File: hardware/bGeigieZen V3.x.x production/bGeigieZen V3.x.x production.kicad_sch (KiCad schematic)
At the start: 14 parts, among them J1 M5 2x15 pin, J10 QI GND, J11 QI charger Plus, J2 Geiger IRover, J3 GPS, J4 Geiger Safepulse, J5 Extra support header, J6 Grove, J8 QI charger ground, J9 QI Plus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

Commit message: Changed the 18650 battery holder to a 1043 Keystone and modified the layout.
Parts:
- BT1: footprint Library:BATTERY_18650-HOLDER -> bGeigieZen:1043
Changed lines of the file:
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@@
 			)
 		)
-		(property "Footprint" "Library:BATTERY_18650-HOLDER"
+		(property "Footprint" "bGeigieZen:1043"
 			(at 83.185 102.108 0)
 			(effects

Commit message: Updated SCL and SDA  and fixed labels  RXs and TX2
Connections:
- net RX2: now also J1.16 (Pin_16), J3.3 (Pin_3); no longer J1.15 (Pin_15), J3.4 (Pin_4)
- net SCL: now also J1.17 (Pin_17), J3.1 (Pin_1); no longer J1.18 (Pin_18), J3.6 (Pin_6)
- net SDA: now also J1.18 (Pin_18), J3.6 (Pin_6); no longer J1.17 (Pin_17), J3.1 (Pin_1)
- net TX2: now also J1.15 (Pin_15), J3.4 (Pin_4); no longer J1.16 (Pin_16), J3.3 (Pin_3)
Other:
- title: bGeigieZen V3.0.3 -> bGeigieZen V3.0.5
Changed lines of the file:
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@@
 	(paper "A4")
 	(title_block
-		(title "bGeigieZen V3.0.3")
-		(date "2024-02-06")
-		(rev "V3.0.3")
+		(title "bGeigieZen V3.0.5")
+		(date "2024-04-07")
+		(rev "V3.0.5")
 		(company "GitHub link at https://github.com/Safecast/bGeigieZen")
 	)
@@
 		(at 125.73 125.73)
 		(diameter 0.3048)
+		(color 0 0 0 0)
+	)
+	(junction
+		(at 173.99 92.71)
+		(diameter 0)
 		(color 0 0 0 0)
 	)
@@
 	)
 	(junction
+		(at 171.45 95.25)
+		(diameter 0)
+		(color 0 0 0 0)
+	)
+	(junction
 		(at 135.89 125.73)
 		(diameter 0.3048)
@@
 	)
 	(junction
-		(at 173.99 95.25)
-		(diameter 0)
-		(color 0 0 0 0)
-	)
-	(junction
-		(at 171.45 92.71)
-		(diameter 0)
-		(color 0 0 0 0)
-	)
-	(junction
 		(at 130.81 78.74)
 		(diameter 0.3048)
@@
 	(wire
 		(pts
-			(xy 173.99 85.09) (xy 173.99 95.25)
+			(xy 173.99 85.09) (xy 173.99 92.71)
 		)
 		(stroke
@@
 	(wire
 		(pts
+			(xy 173.99 92.71) (xy 173.99 96.52)
+		)
+		(stroke
+			(width 0)
+			(type default)
+		)
+	)
+	(wire
+		(pts
 			(xy 74.295 85.09) (xy 83.185 85.09)
 		)
@@
 	(wire
 		(pts
+			(xy 171.45 95.25) (xy 184.15 95.25)
+		)
+		(stroke
+			(width 0)
+			(type default)
+		)
+	)
+	(wire
+		(pts
 			(xy 130.81 78.74) (xy 133.35 78.74)
 		)
@@
 	(wire
 		(pts
+			(xy 171.45 95.25) (xy 171.45 120.65)
+		)
+		(stroke
+			(width 0)
+			(type default)
+		)
+	)
+	(wire
+		(pts
 			(xy 133.35 104.14) (xy 131.445 104.14)
 		)
@@
 	(wire
 		(pts
-			(xy 173.99 95.25) (xy 184.15 95.25)
-		)
-		(stroke
-			(width 0)
-			(type default)
-		)
-	)
-	(wire
-		(pts
 			(xy 113.03 78.74) (xy 116.84 78.74)
 		)
@@
 	(wire
 		(pts
-			(xy 173.99 95.25) (xy 173.99 96.52)
-		)
-		(stroke
-			(width 0)
-			(type default)
-		)
-	)
-	(wire
-		(pts
 			(xy 185.42 56.515) (xy 185.42 66.04)
 		)
@@
 	(wire
 		(pts
-			(xy 171.45 92.71) (xy 171.45 72.39)
-		)
-		(stroke
-			(width 0)
-			(type default)
-		)
-	)
-	(wire
-		(pts
 			(xy 74.295 80.01) (xy 74.295 85.09)
 		)
@@
 	(wire
 		(pts
-			(xy 171.45 92.71) (xy 184.15 92.71)
+			(xy 173.99 92.71) (xy 184.15 92.71)
 		)
 		(stroke
@@
 	(wire
 		(pts
-			(xy 171.45 92.71) (xy 171.45 120.65)
+			(xy 171.45 72.39) (xy 171.45 95.25)
 		)
 		(stroke
@@
 		)
 	)
-	(label "SDA"
+	(label "SCL"
 		(at 146.05 96.52 0)
 		(fields_autoplaced yes)
@@
 		)
 	)
-	(label "TX2"
+	(label "RX2"
 		(at 133.35 93.98 180)
 		(fields_autoplaced yes)
@@
 	)
 	(label "SCL"
-		(at 184.15 92.71 180)
+		(at 180.34 92.71 180)
 		(fields_autoplaced yes)
 		(effects
@@
 		)
 	)
-	(label "SCL"
+	(label "SDA"
 		(at 133.35 96.52 180)
 		(fields_autoplaced yes)
@@
 		)
 	)
-	(label "RX2"
+	(label "TX2"
 		(at 146.05 93.98 0)
 		(fields_autoplaced yes)
@@
 	)
 	(label "SDA"
-		(at 184.15 95.25 180)
-		(fields_autoplaced yes)
-		(effects
+		(at 180.34 95.25 180)
+		(fields_autoplaced yes)
+		(effects

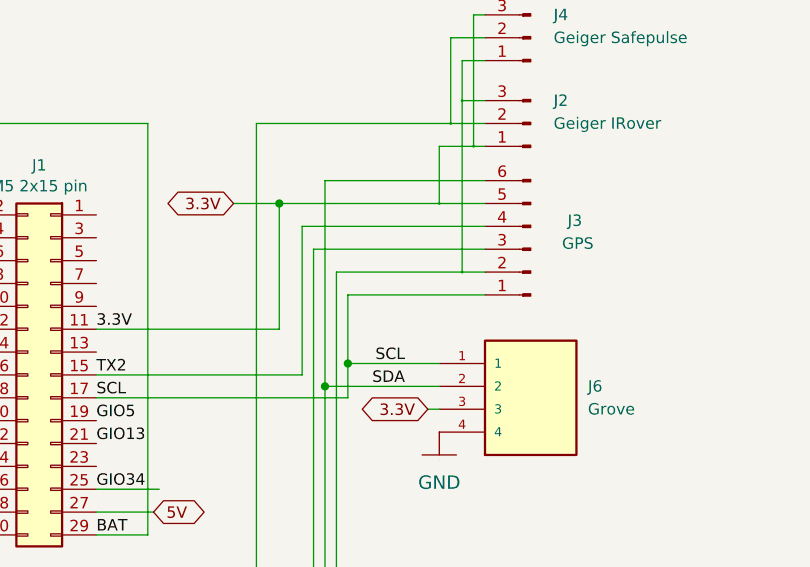
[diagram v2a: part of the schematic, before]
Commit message: Swapped SDA and SCL lines on GPS
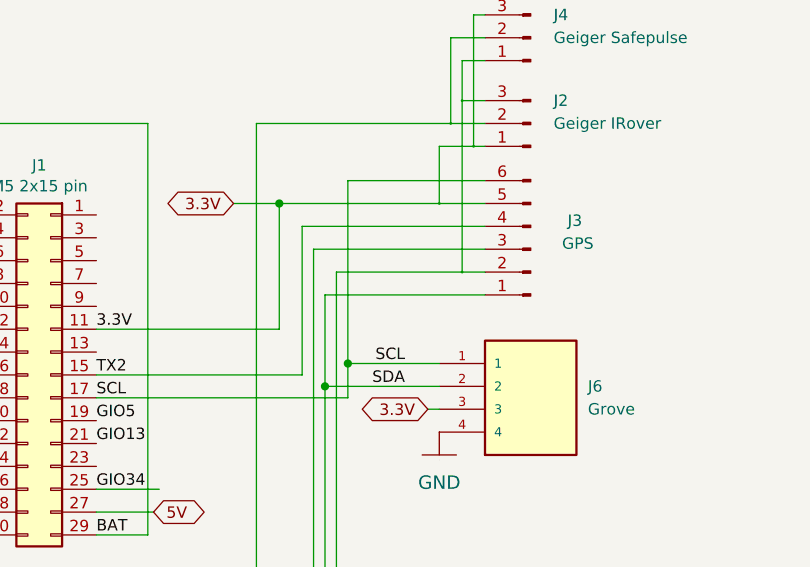
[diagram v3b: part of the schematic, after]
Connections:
- net SCL: now also J3.6 (Pin_6); no longer J3.1 (Pin_1)
- net SDA: now also J3.1 (Pin_1); no longer J3.6 (Pin_6)
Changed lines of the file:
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@@
-	(wire
-		(pts
-			(xy 173.99 85.09) (xy 173.99 92.71)
-		)
-		(stroke
-			(width 0)
-			(type default)
-		)
-	)
 	(wire
 		(pts
@@
 	(wire
 		(pts
-			(xy 189.23 85.09) (xy 173.99 85.09)
-		)
-		(stroke
-			(width 0)
-			(type default)
-		)
-	)
-	(wire
-		(pts
 			(xy 69.85 87.63) (xy 69.85 125.73)
 		)
@@
 	(wire
 		(pts
-			(xy 171.45 72.39) (xy 189.23 72.39)
+			(xy 173.99 72.39) (xy 173.99 92.71)
 		)
 		(stroke
@@
 	(wire
 		(pts
+			(xy 171.45 85.09) (xy 189.23 85.09)
+		)
+		(stroke
+			(width 0)
+			(type default)
+		)
+	)
+	(wire
+		(pts
 			(xy 120.65 73.66) (xy 120.65 66.04)
 		)
@@
 	(wire
 		(pts
+			(xy 173.99 72.39) (xy 189.23 72.39)
+		)
+		(stroke
+			(width 0)
+			(type default)
+		)
+	)
+	(wire
+		(pts
 			(xy 69.85 80.01) (xy 74.295 80.01)
 		)
@@
 	(wire
 		(pts
-			(xy 171.45 72.39) (xy 171.45 95.25)
-		)
-		(stroke
+			(xy 171.45 85.09) (xy 171.45 95.25)
+		)
+		(stroke

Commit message: Update Board V3.0.5
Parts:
- BT1: footprint bGeigieZen:1043 -> bGeigieZen:BATTERY_18650-HOLDER
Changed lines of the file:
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@@
 			)
 		)
-		(property "Footprint" "bGeigieZen:1043"
+		(property "Footprint" "bGeigieZen:BATTERY_18650-HOLDER"
 			(at 83.185 102.108 0)
 			(effects

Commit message: Renamed V3.0.5a boards to V3.0.6 .
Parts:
- BT1: value 3.7 V Lipo -> 3.7 V Lipo
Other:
- title: bGeigieZen V3.0.5 -> bGeigieZen V3.0.6
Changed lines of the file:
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@@
 (kicad_sch
-	(version 20240417)
+	(version 20240602)
 	(generator "eeschema")
 	(generator_version "8.99")
 	(paper "A4")
 	(title_block
-		(title "bGeigieZen V3.0.5")
-		(date "2024-06-04")
-		(rev "V3.0.5")
+		(title "bGeigieZen V3.0.6")
+		(date "2024-06-16")
+		(rev "V3.0.6")
 		(company "GitHub link at https://github.com/Safecast/bGeigieZen")
 	)
@@
 			)
 		)
-		(property "Value" " 3.7 V Lipo"
+		(property "Value" "3.7 V Lipo"
 			(at 74.6252 113.1062 0)
 			(effects

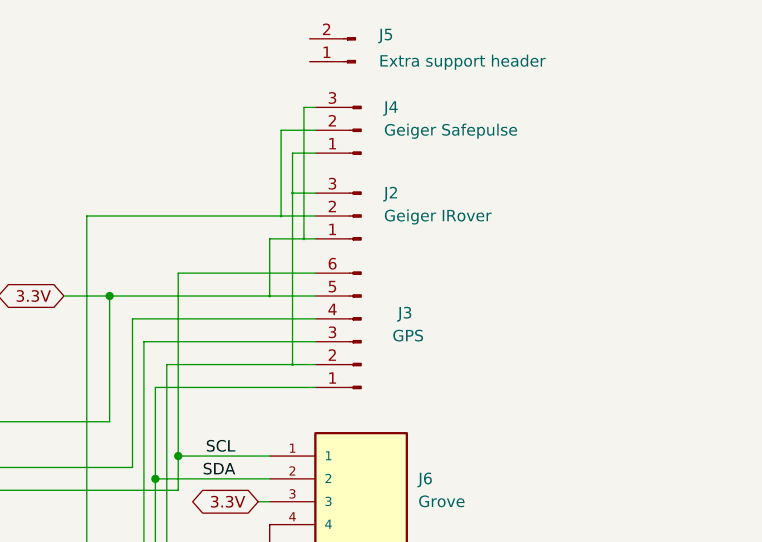
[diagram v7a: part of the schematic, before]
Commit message: remove Irover pins. The Irover fits now at the same location as the safeppulse.
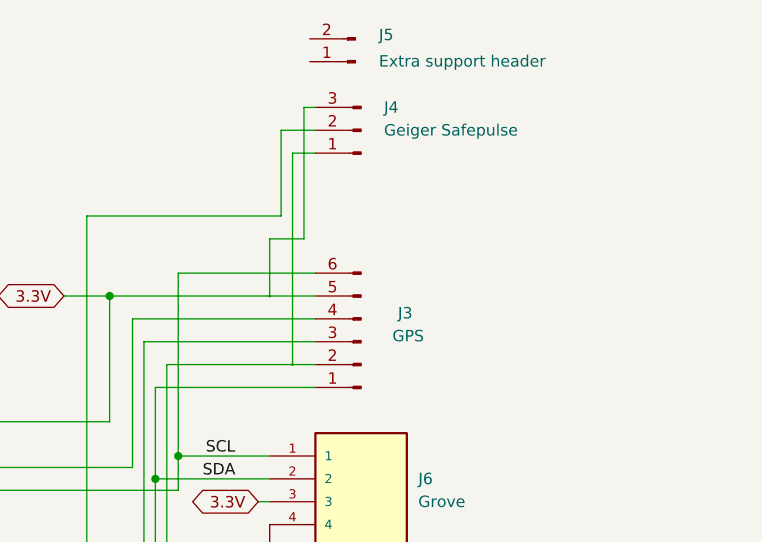
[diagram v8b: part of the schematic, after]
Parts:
- removed J2: Geiger IRover, Connector_PinHeader_2.54mm:PinHeader_1x03_P2.54mm_Vertical, symbol Connector:Conn_01x03_Male
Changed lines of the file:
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@@
 	(title_block
 		(title "bGeigieZen V3.0.6")
-		(date "2024-06-16")
+		(date "2024-06-18")
 		(rev "V3.0.6")
 		(company "GitHub link at https://github.com/Safecast/bGeigieZen")
@@
 	)
 	(junction
-		(at 186.69 63.5)
-		(diameter 0.3048)
-		(color 0 0 0 0)
-	)
-	(junction
-		(at 185.42 66.04)
-		(diameter 0.3048)
-		(color 0 0 0 0)
-	)
-	(junction
 		(at 69.85 71.12)
 		(diameter 0.3048)
@@
 	)
 	(junction
-		(at 187.96 68.58)
-		(diameter 0.3048)
-		(color 0 0 0 0)
-	)
-	(junction
 		(at 171.45 95.25)
 		(diameter 0)
@@
 	(wire
 		(pts
-			(xy 189.23 66.04) (xy 185.42 66.04)
-		)
-		(stroke
-			(width 0)
-			(type solid)
-		)
-	)
-	(wire
-		(pts
 			(xy 146.05 96.52) (xy 173.99 96.52)
 		)
@@
 	(wire
 		(pts
-			(xy 186.69 82.55) (xy 186.69 63.5)
+			(xy 186.69 59.055) (xy 186.69 82.55)
 		)
 		(stroke
@@
 	(wire
 		(pts
-			(xy 187.96 68.58) (xy 189.23 68.58)
-		)
-		(stroke
-			(width 0)
-			(type solid)
-		)
-	)
-	(wire
-		(pts
 			(xy 129.54 99.06) (xy 133.35 99.06)
 		)
@@
 	(wire
 		(pts
-			(xy 186.69 63.5) (xy 186.69 59.055)
-		)
-		(stroke
-			(width 0)
-			(type solid)
-		)
-	)
-	(wire
-		(pts
 			(xy 166.37 74.93) (xy 166.37 88.9)
 		)
@@
 			(width 0)
 			(type default)
-		)
-	)
-	(wire
-		(pts
-			(xy 186.69 63.5) (xy 189.23 63.5)
-		)
-		(stroke
-			(width 0)
-			(type solid)
 		)
 	)
@@
 					(unit 1)
 				)
-			)
-		)
-	)
-	(symbol
-		(lib_id "Connector:Conn_01x03_Male")
-		(at 194.31 66.04 180)
-		(unit 1)
-		(exclude_from_sim no)
-		(in_bom yes)
-		(on_board yes)
-		(dnp no)
-		(property "Reference" "J2"
-			(at 196.85 63.5 0)
-			(effects
-				(font
-					(size 1.27 1.27)
-				)
-				(justify right)
-			)
-		)
-		(property "Value" "Geiger IRover"
-			(at 196.85 66.04 0)
-			(effects
-				(font
-					(size 1.27 1.27)
-				)
-				(justify right)
-			)
-		)
-		(property "Footprint" "Connector_PinHeader_2.54mm:PinHeader_1x03_P2.54mm_Vertical"
-			(at 194.31 66.04 0)
-			(effects
-				(font
-					(size 1.27 1.27)
-				)
-				(hide yes)
-			)
-		)
-		(property "Datasheet" "~"
-			(at 194.31 66.04 0)
-			(effects
-				(font
-					(size 1.27 1.27)
-				)
-				(hide yes)
-			)
-		)
-		(property "Description" ""
-			(at 194.31 66.04 0)
-			(effects
-				(font
-					(size 1.27 1.27)
-				)
-				(hide yes)
-			)
-		)
-		(pin "1"
-		)
-		(pin "2"
-		)
-		(pin "3"
-		)
-		(instances
-			(project "bGeigieZen V3.x.x production"
-				(path "/c2e3a215-6a49-419d-95d1-595f35b17280"
-					(reference "J2")
-					(unit 1)
-				)
